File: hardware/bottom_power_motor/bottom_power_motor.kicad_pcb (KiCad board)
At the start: 2 copper layers, 52 x 52 mm, 104 parts, among them J1 Power/Motor 6p, J2 J_STK_A, J3 J_STK_B, Q1 P-FET 40V 30A, U1 L78L12, U2 TPS54360, U2_CB 100n, U2_CO 47u, U2_CZ 3n3, U2_D 60V 3A, U2_L 10u, U2_RC 10k, U2_RH 53k6, U2_RL 10k2, U2_RT_R 100k, U3 TLV62569, U4 TPS54360, U4_CB 100n, U4_CO 22u, U4_CZ 3n3, U4_D 60V 3A, U4_L 33u, U4_RC 10k, U4_RH 68k1, U4_RL 10k0, U4_RT_R 100k

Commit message: Blockierstrom gemessen: 1,6 A statt 25 A - Auslegung neu gerechnet
Am 17.08.2026 mit blockiertem Abtrieb gemessen: 1,6 A bei 24 V, Netzteil mit
5 A Reserve, also keine Strombegrenzung. Daraus R_Anker = 15 Ohm. Die Messung
vom Vortag (0,116 A bei 2 V, 17,2 Ohm) bestaetigt das aus einem zwoelffach
anderen Betriebspunkt - die Zwischenbewertung "unbrauchbar" war falsch und ist
zurueckgenommen. Aufgeloest ist damit auch der Widerspruch zum Typenschild:
24 V an 15 Ohm ergeben maximal 38 W, die 100 W sind die Netzteilempfehlung der
Anlage, nicht die Aufnahme eines Motors.

GEAENDERTE WERTE - kein Layout betroffen:

  Shunt R_M1_SH/R_M2_SH   1 mOhm -> 5 mOhm    (gleicher Footprint)
  Trip-Teiler R8          40k2   -> 30k9      (+/-22 A -> +/-4,0 A)
  Sicherung F1            15 A   -> 6,3 A traege
  Firmware-Skalierung     20 A/V -> 4 A/V

Der Shunt wird groesser, nicht kleiner: Er bestimmt nicht die Belastbarkeit,
sondern die Aufloesung. Am 1-mOhm-Shunt lagen zwischen Fahrt und Anschlag nur
30-65 mV, in der Groessenordnung des ADC-Rauschens. Mit 5 mOhm sind es
150-325 mV bei 0,25 V/A und +/-6,6 A Messbereich; die Verlustleistung betraegt
bei 2 A ganze 20 mW.

Die Trip-Schwelle muss UEBER dem Blockierstrom liegen, weil der Anschlag ohne
Endschalter ein normaler Betriebszustand ist - der Laden faehrt bei jeder Fahrt
kurz dagegen. 4,0 A gibt Faktor 2,5 Reserve, ein echter Kurzschluss liegt
Groessenordnungen darueber.

FEHLER IN DER FIRMWARE MITGEFUNDEN: Der Nullpunkt des INA240 wurde nirgends
abgezogen. Der Sensor haette im Stillstand 6,6 A gemeldet statt 0 A. Jetzt
Betragsbildung um einen einstellbaren Nullpunkt (Vorgabe 1,65 V), damit auch
die Richtungsumkehr am Inline-Shunt kein Vorzeichen mehr erzeugt.

WAS DIE MESSUNG ERLEDIGT: Punkt 1 (Blockierstrom), Punkt 2 (Steckverbinder -
Micro-Fit 3.0 reicht, Mini-Fit Jr. nicht noetig) und die Verschaerfung von
Punkt 3. Der Summenstrom faellt von 9 A auf 3,9 A im unguenstigsten Fall.
Ein Anlaufstrom ueber dem Blockierstrom existier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
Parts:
- R8: value 40k2 -> 30k9
- R_M1_SH, R_M2_SH: value 1m0 1W -> 5m0 1W
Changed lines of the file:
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@@
 			)
 		)
-		(property "Value" "1m0 1W"
+		(property "Value" "5m0 1W"
 			(at 0 2.62 90)
 			(layer "F.Fab")
@@
 			)
 		)
-		(property "Value" "40k2"
+		(property "Value" "30k9"
 			(at 0 1.43 0)
 			(layer "F.Fab")
@@
 			)
 		)
-		(property "Value" "1m0 1W"
+		(property "Value" "5m0 1W"
 			(at 0 -2.62 180)
 			(layer "B.Fab")

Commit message: Reserve nachgerechnet: Wind, Messfehler - und ein Fehler am Komparator
Nachgegangen der Frage, wie sicher der gemessene Blockierstrom ist und was bei
Wind passiert. Drei Ergebnisse, docs/11 Abschnitt 6 neu.

1) DER BLOCKIERSTROM IST EINE HARTE OBERGRENZE, keine Lastannahme. Bei
   blockiertem Laeufer ist die Gegenspannung null, also I = U/R. Ein Drehmoment
   kommt in der Gleichung nicht vor - Wind kann den Motor nur langsamer machen,
   und langsamer heisst naeher an 1,6 A, nie darueber. Ueberschritten wird die
   Grenze nur beim Umpolen eines noch drehenden Motors (bis 3,2 A), und dagegen
   stehen 300 ms Stoppause und die Selbsthemmung des Schneckengetriebes.

   Der Trip liegt mit 4,4 A ueber allen drei denkbaren Faellen.

2) TRIP-TEILER BLEIBT BEI 40k2 statt der gestern eingesetzten 30k9. Der
   groessere Shunt nimmt die Schwelle von allein von 22 A auf 4,4 A mit - ein
   Bauteil weniger geaendert, und die zusaetzliche Reserve kostet nichts, weil
   zwischen 4 und 5 A auf dieser Platine ohnehin nichts gefaehrdet ist. Damit
   traegt die Auslegung einen Messfehler von Faktor 2,5.

   Gegenprobe fuer Faktor 2 (3,2 A statt 1,6 A) in Abschnitt 6.2: Es reagieren
   genau zwei Positionen, und die Sicherung ist dabei kein Risiko, sondern der
   Melder - sie fliegt beim ersten beidseitigen Anschlag, harmlos und sofort
   sichtbar.

   Billige dritte Bestaetigung: M6 mit dem Multimeter ist bei 15 Ohm endlich
   brauchbar (Zuleitungen unter 3 % statt der Haelfte). Erwartet 14-17 Ohm,
   zwei Minuten, kein Blockieren.

3) WIND IST EIN MECHANISCHES PROBLEM. Ueberschlag fuer 0,84 m2 Flaeche: Ab
   etwa 40 km/h uebersteigt das Windmoment am Band die 25 Nm des Motors, bei
   90 km/h steht das Fuenffache dagegen. Elektrisch aendert das nichts, die
   Endlagenerkennung bricht aber in beide Richtungen: Gegenwind sieht aus wie
   ein Anschlag, Rueckenwind schlaegt den Fluegel bei NIEDRIGEREM Strom als
   normal gegen den Anschlag. Punkt 58 mit drei Gegenmassnahmen, davon die
   w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
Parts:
- R8: value 30k9 -> 40k2
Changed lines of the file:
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@@
 			)
 		)
-		(property "Value" "30k9"
+		(property "Value" "40k2"
 			(at 0 1.43 0)
 			(layer "F.Fab")

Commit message: TLV3702 statt LM393; Auslegung auf den kleinsten gemessenen Wert (14 Ohm)
ZWEI SACHEN IN EINEM COMMIT, weil beide aus derselben Messreihe kommen.

1) M6 vollstaendig: 16,5 / 20 / 14 Ohm. Die Streuung ist der erwartete
   Buersteneffekt - je nach Laeuferstellung liegen unterschiedlich viele
   Lamellen im Strompfad. Fuer die Auslegung zaehlt das Minimum, und das sind
   jetzt 14 Ohm statt der 15,0 Ohm aus M3. Damit steigt der Blockierstrom von
   1,6 auf 1,7 A, der Summenpfad von 3,9 auf 4,1 A und die Maximalaufnahme je
   Motor von 38 auf 41 W.

   Kein Bauteil aendert sich: Ausgelegt war ohnehin auf 2 A, der Trip liegt bei
   4,4 A (Faktor 2,6), die Sicherung bei 6,3 A. Die Zahlen sind nur ueberall
   konsistent nachgezogen.

   Damit ist der Blockierstrom dreifach unabhaengig bestaetigt - 2 V, 24 V
   blockiert, Multimeter - und der Faktor-2-Irrtum ausgeschlossen.

2) Punkt 57 geloest, und zwar OHNE die geroutete Platine anzufassen.

   Der Weg ueber 5V_SYS, den der Nutzer zunaechst gewaehlt hatte, scheiterte an
   der Geometrie: Das Netz liegt komplett auf der linken Boardhaelfte, die
   Komparatoren rechts - 27,3 bzw. 36,0 mm entfernt, zwei lange Bahnen ueber
   985 vorhandene Segmente. 12V_GATE waere mit 3-7 mm nah, ist aber die
   lauteste Schiene der Platine, und der Komparator hat keinen eigenen
   Abblockkondensator.

   Gewaehlt: TLV3702. Rail-to-Rail-Eingang, Open-Drain, SOIC-8 im
   Standard-Pinout eines dualen Komparators. Gleicher Footprint, gleiche Netze,
   keine Leiterbahn angefasst, DRC unveraendert (228 Meldungen, alle
   Bestueckungsdruck; 61 offene Verbindungen wie zuvor). Er bleibt an 3,3 V und
   damit auf derselben Schiene wie die INA240-Referenz, was die ratiometrische
   Kopplung der Trip-Schwelle erhaelt. Mit rund 5 us ist er langsamer als der
   LM393 - hier ein Vorteil, weil der Komparator das ungefilterte Sense-Signal
   sieht und an einem Latch haengt (Punkt 59).

   ACHTUNG fuer die Bestellung: KiCad 10 bringt kein TLV-Symbol mit, im
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
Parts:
- UM1_CMP, UM2_CMP: value LM393 -> TLV3702
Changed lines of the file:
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@@
 			)
 		)
-		(property "Value" "LM393"
+		(property "Value" "TLV3702"
 			(at 0 3.4 0)
 			(layer "F.Fab")
@@
 			)
 		)
-		(property "Value" "LM393"
+		(property "Value" "TLV3702"
 			(at 0 -3.4 -90)
 			(layer "B.Fab")

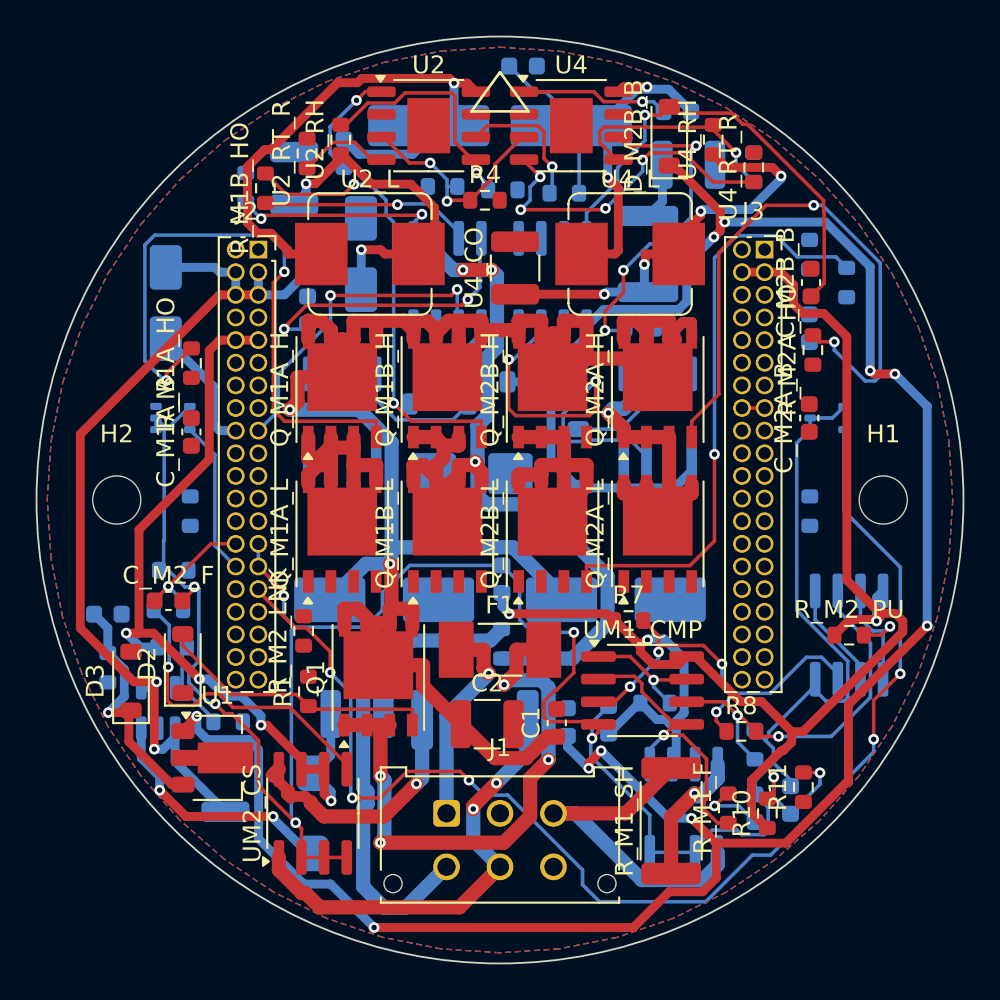
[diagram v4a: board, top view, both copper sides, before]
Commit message: Regelwerk und Router in Deckung gebracht: 41 Clearance-Fehler auf 5
Drei getrennte Ursachen, alle aus derselben Wurzel - die Regeln, nach denen
geroutet wurde, waren nicht die, nach denen geprueft wurde.

1) DIE PROJEKTDATEIEN FORDERTEN 0,2 mm. docs/05 nennt 0,15 mm als gueltige
   Regel und warnt sogar ausdruecklich davor, dass KiCad ohne .kicad_pro auf
   0,2 mm zurueckfaellt und dann Verletzungen meldet, die keine sind. Genau
   dieser Wert stand aber IN den Projektdateien. Auf 0,15 korrigiert, in allen
   drei Projekten.

   Bottom  clearance  41 -> 5
   Mid     clearance   1 -> 0

2) DER RANDKEEPOUT GALT NUR FUER F UND B. _edge_ring() hatte die Lagenliste
   fest verdrahtet; auf In1/In2 routete Freerouting bis an die Kante. Daher
   vier copper_edge_clearance-Verletzungen, die es auf den Aussenlagen nicht
   gab. Die Liste kommt jetzt aus dem DSN.

3) FREEROUTING UNTERSCHREITET SEINE VORGABE. Bei 150 um Anweisung kamen auf
   In1.Cu real 114 bis 144 um heraus - die fuenf verbliebenen Verletzungen
   sind alle von dieser Art, alle zwischen 24V_F und 3V3_SYS auf engem Raum.
   Die Klassen fordern jetzt 200 statt 150 um (Mid und Top 250 statt 200),
   damit auch das Ergebnis ueber 0,15 mm bleibt. Bahnbreiten unveraendert.

Punkt 2 und 3 wirken erst beim naechsten Lauf.

Co-Authored-By: Claude Opus 5 (1M context) <noreply@anthropic.com>
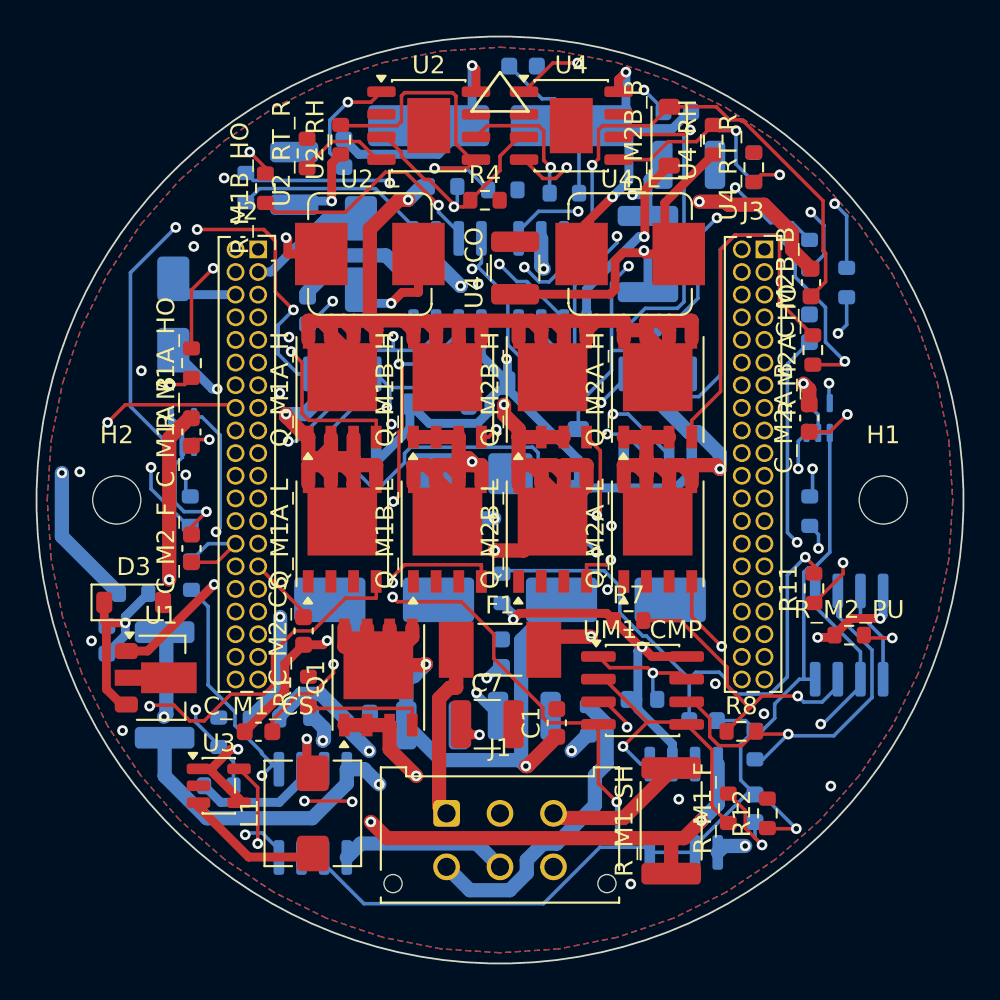
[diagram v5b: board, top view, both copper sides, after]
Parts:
- C2, D2, R10, R_M2_LNK, UM2_CS: moved to B.Cu
- C7, C_M1_CS, C_M2_CS, L1, R12, U3: moved to F.Cu
- moved R12 36.0 mm to (15.0, 17.6), turned to 90 degrees
- moved C_M1_CS 19.7 mm to (-13.5, 13.0), turned to 0 degrees
- moved R10 19.5 mm to (0.11, 4.96)
- moved R_M2_SH 17.5 mm to (-18.8, 10.4), turned to 90 degrees
- moved C8 17.2 mm to (1.36, 12.1), turned to 0 degrees
- moved C_M2_CS 11.5 mm to (-11.0, 7.35)
- moved R11 11.2 mm to (17.6, 4.96)
- moved D2 9.32 mm to (-8.95, 12.1), turned to 0 degrees
- moved R5 8.21 mm to (-15.8, 16.0)
- moved C7 7.33 mm to (-0.72, 12.6)
- moved C10 6.63 mm to (11.4, 12.4), turned to 0 degrees
- moved R_M1_LNK 6.50 mm to (4.95, 12.4)
- moved U3 5.53 mm to (-15.8, 16.0), turned to 0 degrees
- moved U1 5.50 mm to (-19.0, 9.97)
- moved R_M2_LNK 5.41 mm to (-13.2, 12.3), turned to 0 degrees
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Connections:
- net RADAR_INT renamed PRESENCE_INT
- net UART_RADAR_RX renamed UART_AUX_RX
- net UART_RADAR_TX renamed UART_AUX_TX
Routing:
- net M1_INA: track 0.00 -> 100.6 mm, vias 0 -> 4
- net M1_SWA: track 23.9 -> 114.1 mm, vias 1 -> 5
- net M2_SWA: track 32.5 -> 99.8 mm, vias 2 -> 3
- net 24V_PROT: track 110.5 -> 177.3 mm, vias 2 -> 5
- net M2_SD: track 21.7 -> 86.5 mm, vias 2 -> 6
- net TRIP_RST: track 0.00 -> 63.6 mm, vias 0 -> 1
- net I_SENSE1: track 3.70 -> 63.5 mm
- net M1A_HO_G: track 0.00 -> 58.4 mm, vias 0 -> 4
- net M2_SWB: track 14.0 -> 70.3 mm, vias 0 -> 5
- net M2_INB: track 0.00 -> 47.6 mm, vias 0 -> 2
- net M2_INA: track 0.00 -> 47.2 mm, vias 0 -> 2
- net M1_SD: track 0.00 -> 46.6 mm, vias 0 -> 2
- net U4_CZ_N: track 0.00 -> 46.4 mm, vias 0 -> 2
- net M1B_LO_GT: track 0.00 -> 42.4 mm, vias 0 -> 3
- net M1A_LO_GT: track 0.00 -> 40.5 mm, vias 0 -> 3
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- added copper zone on In1.Cu, net PGND
- added copper zone on In2.Cu, net PGND
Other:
- copper layers 2 -> 4

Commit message: Waermefallen: 65 starved_thermal auf null, zwei getrennte Massnahmen
INNEN VOLLE ANBINDUNG. Auf den Innenlagen ist die Massefl. durch die
Leiterbahnen zerschnitten; ein Pad bekommt dort oft nur einen Steg statt der
geforderten zwei. Waermefallen existieren fuers Handloeten, und innen wird
nicht geloetet - also volle Anbindung auf In1/In2, Waermefallen bleiben aussen,
weil die Durchsteckteile von Hand kommen.

  starved_thermal   Bottom 30->21   Mid 19->14   Top 15->8

MIN_RESOLVED_SPOKES VON 2 AUF 1. Der Rest liegt aussen, wo die Flaeche
ebenfalls zerschnitten ist und ein zweiter Steg geometrisch nicht mehr
passt. Zwei Stege sind eine Empfehlung fuer gleichmaessiges Erwaermen, kein
elektrisches Erfordernis; ein Steg plus umgebende Flaeche traegt den
Massestrom dieser Boards um Groessenordnungen. Bewusste Regelentscheidung,
nicht stillschweigend - aufgenommen in docs/06.

  starved_thermal   Bottom 21->0    Mid 14->0    Top 8->0

STAND DER DREI BOARDS

              Segmente  offene Signale  Kupferfehler
  mid_logic       637         2              0
  bottom_power   1376         8              2   (0,1476 und 0,1017 statt 0,15)
  top_ui          193        11             11   (alle an der USB-C-Buchse J1)

Co-Authored-By: Claude Opus 5 (1M context) <noreply@anthropic.com>
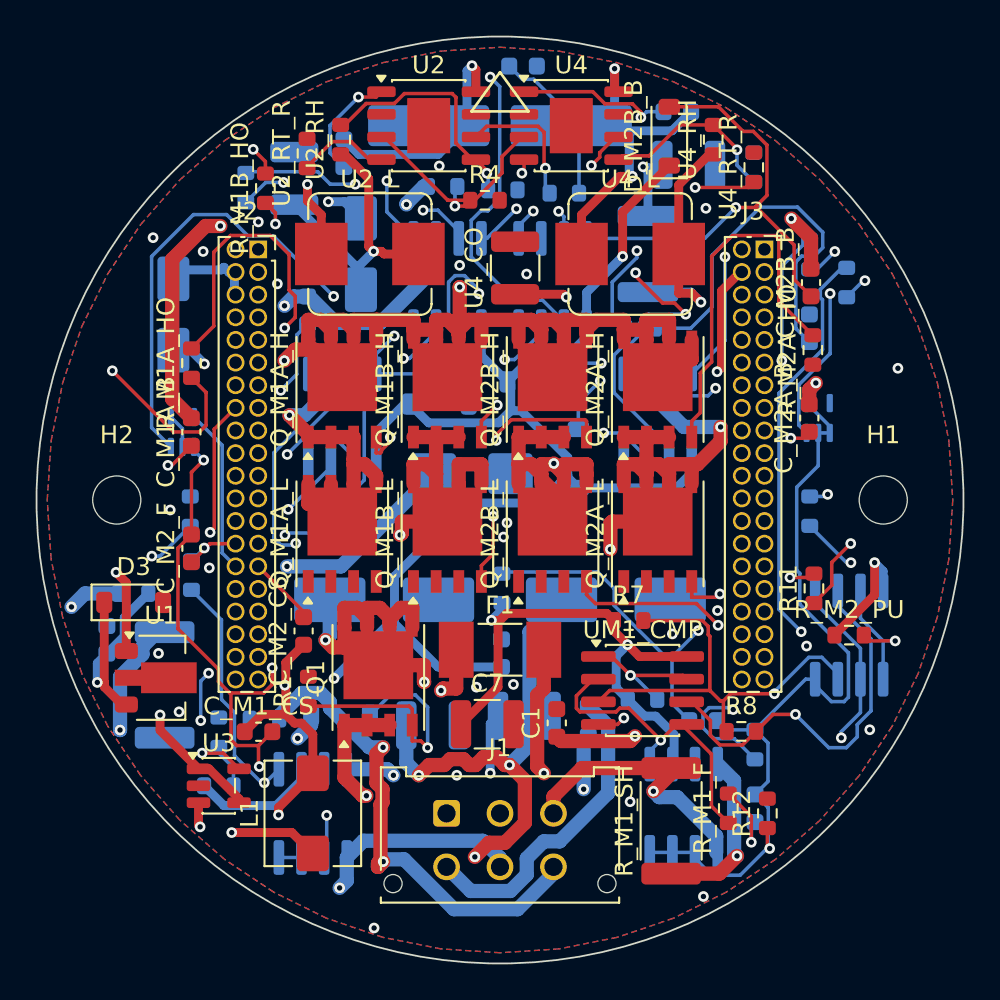
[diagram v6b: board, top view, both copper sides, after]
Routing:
- net M1_INA: track 100.6 -> 38.6 mm, vias 4 -> 2
- net HW_TRIP2: track 54.9 -> 0.00 mm, vias 2 -> 0
- net M1_SWA: track 114.1 -> 161.0 mm
- net M2_SD: track 86.5 -> 43.1 mm, vias 6 -> 3
- net M1A_LO_GT: track 40.5 -> 0.00 mm, vias 3 -> 0
- net M2B_HO_GT: track 32.3 -> 64.4 mm, vias 2 -> 4
- net M1A_LO_G: track 32.7 -> 61.7 mm, vias 3 -> 5
- net M2_SWB: track 70.3 -> 42.4 mm, vias 5 -> 3
- net TRIP_RST: track 63.6 -> 91.4 mm, vias 1 -> 2
- net M1A_HO_G: track 58.4 -> 85.7 mm, vias 4 -> 5
- net M2A_HO_G: track 25.2 -> 0.00 mm, vias 1 -> 0
- net 3V3_SYS: track 125.7 -> 150.3 mm
- net U4_CZ_N: track 46.4 -> 22.0 mm, vias 2 -> 0
- net AGND: track 148.3 -> 129.1 mm, vias 7 -> 6
- net 12V_GATE: track 110.2 -> 94.4 mm, vias 4 -> 3
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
